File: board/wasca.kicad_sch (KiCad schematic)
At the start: 145 parts, among them CN1 UC09-0B16F00P11, CN2 CARTRIDGE_EDGE_CONNECTOR, CN3 TFP09-2-12B, CN4 SD-CARD 11P, CN5 2.54-1*8P母环保, SW1 TS-1101-C-W, SW2 TS-1101-C-W, U1 SN74LVC1T45DBVR, U10 74ALVC164245DGG:11-JSM, U11 W9825G6KH-6, U12 W9825G6KH-6, U13 SY8008CAAC, U14 SY8008CAAC, U15 XC6206P252MR, U16 LFE5U-25F-6BG256I, U17 P25Q16SH-SSH-IR, U2 SN74LVC1T45DBVR, U3 P25Q16SH-SSH-IR, U4 SN74LVC1T45DBVR, U5 SN74LVC1T45DBVR, U6 SN74LVC1T45DBVR, U7 74ALVC164245DGG:11-JSM, U8 74ALVC164245DGG:11-JSM, U9 RP2040, Y1 X322512MSB4SI, Y2 SX2M25.000M20F30TNN

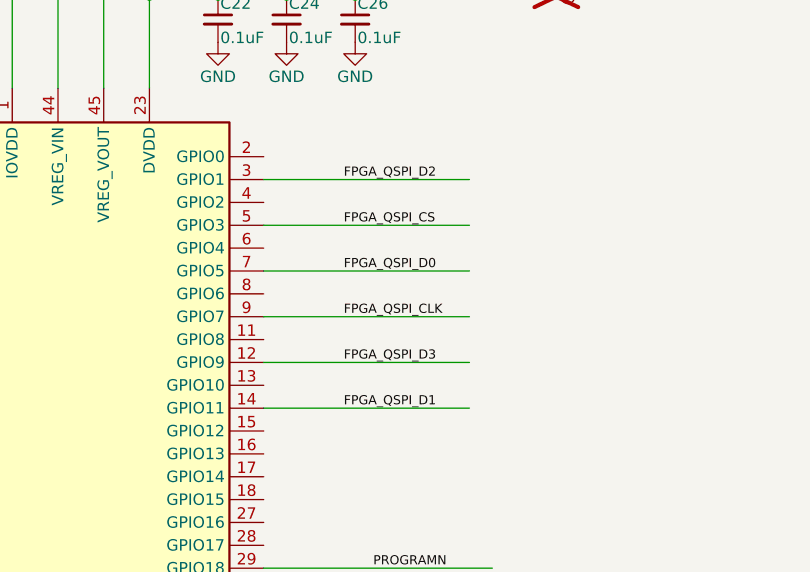
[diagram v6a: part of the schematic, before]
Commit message: Moving RP2040 to front to simplify 2-stage assembly (front at fab, back manually).
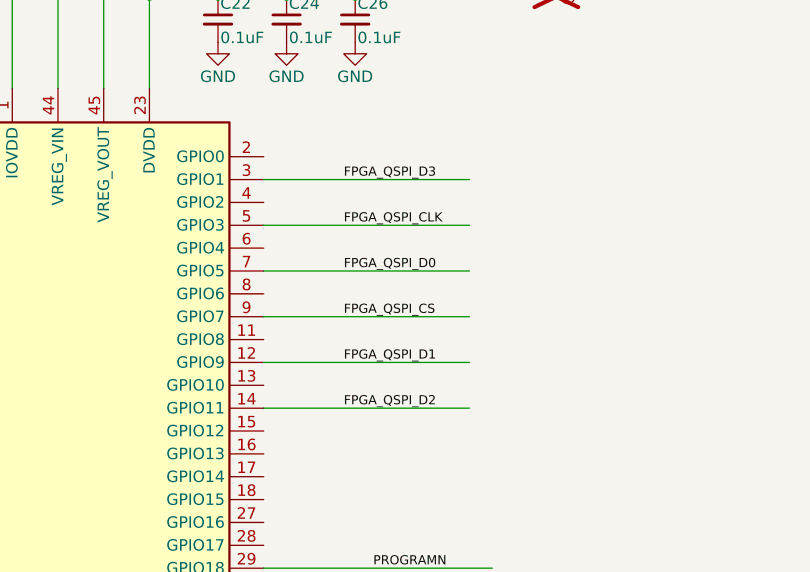
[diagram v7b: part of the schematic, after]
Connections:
- net FPGA_QSPI_CLK: now also U9.5 (GPIO3); no longer U9.9 (GPIO7)
- net FPGA_QSPI_CS: now also U9.9 (GPIO7); no longer U9.5 (GPIO3)
- net FPGA_QSPI_D1: now also U9.12 (GPIO9); no longer U9.14 (GPIO11)
- net FPGA_QSPI_D2: now also U9.14 (GPIO11); no longer U9.3 (GPIO1)
- net FPGA_QSPI_D3: now also U9.3 (GPIO1); no longer U9.12 (GPIO9)
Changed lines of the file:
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@@
 	(wire
 		(pts
+			(xy 250.19 575.31) (xy 273.05 575.31)
+		)
+		(stroke
+			(width 0)
+			(type default)
+		)
+	)
+	(wire
+		(pts
 			(xy 1078.23 104.14) (xy 1056.64 104.14)
 		)
@@
 	(wire
 		(pts
+			(xy 250.19 580.39) (xy 273.05 580.39)
+		)
+		(stroke
+			(width 0)
+			(type default)
+		)
+	)
+	(wire
+		(pts
 			(xy 190.5 445.77) (xy 190.5 439.42)
 		)
@@
 	(wire
 		(pts
+			(xy 250.19 554.99) (xy 273.05 554.99)
+		)
+		(stroke
+			(width 0)
+			(type default)
+		)
+	)
+	(wire
+		(pts
 			(xy 509.27 85.09) (xy 509.27 91.44)
 		)
@@
 	(wire
 		(pts
-			(xy 250.19 575.31) (xy 273.05 575.31)
-		)
-		(stroke
-			(width 0)
-			(type default)
-		)
-	)
-	(wire
-		(pts
 			(xy 938.53 283.21) (xy 960.12 283.21)
 		)
@@
 	(wire
 		(pts
-			(xy 250.19 580.39) (xy 273.05 580.39)
-		)
-		(stroke
-			(width 0)
-			(type default)
-		)
-	)
-	(wire
-		(pts
 			(xy 612.14 85.09) (xy 621.03 85.09)
 		)
@@
 	(wire
 		(pts
-			(xy 250.19 560.07) (xy 273.05 560.07)
-		)
-		(stroke
-			(width 0)
-			(type default)
-		)
-	)
-	(wire
-		(pts
 			(xy 233.68 153.67) (xy 252.73 153.67)
 		)
@@
 	(wire
 		(pts
-			(xy 250.19 554.99) (xy 273.05 554.99)
-		)
-		(stroke
-			(width 0)
-			(type default)
-		)
-	)
-	(wire
-		(pts
 			(xy 1055.37 405.13) (xy 1055.37 407.67)
 		)
@@
 	(wire
 		(pts
-			(xy 250.19 570.23) (xy 273.05 570.23)
-		)
-		(stroke
-			(width 0)
-			(type default)
-		)
-	)
-	(wire
-		(pts
 			(xy 621.03 74.93) (xy 621.03 76.2)
 		)
@@
 		)
 	)
+	(wire
+		(pts
+			(xy 250.19 570.23) (xy 273.05 570.23)
+		)
+		(stroke
+			(width 0)
+			(type default)
+		)
+	)
 	(bus
 		(pts
@@
 	(wire
 		(pts
+			(xy 250.19 560.07) (xy 273.05 560.07)
+		)
+		(stroke
+			(width 0)
+			(type default)
+		)
+	)
+	(wire
+		(pts
 			(xy 542.29 74.93) (xy 542.29 80.01)
 		)
@@
 		)
 	)
-	(label "FPGA_QSPI_D1"
-		(at 259.08 580.39 0)
-		(effects
-			(font
-				(size 1.016 1.016)
-			)
-			(justify left bottom)
-		)
-	)
-	(label "FPGA_QSPI_D3"
-		(at 259.08 575.31 0)
-		(effects
-			(font
-				(size 1.016 1.016)
-			)
-			(justify left bottom)
-		)
-	)
 	(label "ABUS_3V_A22"
 		(at 238.76 158.75 0)
@@
 		)
 	)
-	(label "FPGA_QSPI_D2"
-		(at 259.08 554.99 0)
-		(effects
-			(font
-				(size 1.016 1.016)
-			)
-			(justify left bottom)
-		)
-	)
 	(label "+5V_SATURN"
 		(at 72.39 363.22 180)
@@
 		)
 	)
+	(label "FPGA_QSPI_D1"
+		(at 259.08 575.31 0)
+		(effects
+			(font
+				(size 1.016 1.016)
+			)
+			(justify left bottom)
+		)
+	)
 	(label "SDRAM2_A2"
 		(at 750.57 133.35 180)
@@
 		)
 	)
+	(label "FPGA_QSPI_D2"
+		(at 259.08 580.39 0)
+		(effects
+			(font
+				(size 1.016 1.016)
+			)
+			(justify left bottom)
+		)
+	)
 	(label "FPGA_QSPI_CS"
 		(at 741.68 74.93 0)
@@
 		)
 	)
+	(label "FPGA_QSPI_CS"
+		(at 259.08 570.23 0)
+		(effects
+			(font
+				(size 1.016 1.016)
+			)
+			(justify left bottom)
+		)
+	)
 	(label "ABUS_3V_D12"
 		(at 255.27 325.12 0)
@@
 		)
 	)
+	(label "FPGA_QSPI_CLK"
+		(at 259.08 560.07 0)
+		(effects
+			(font
+				(size 1.016 1.016)
+			)
+			(justify left bottom)
+		)
+	)
 	(label "SDRAM1_A5"
 		(at 410.21 300.99 180)
@@
 		)
 	)
+	(label "FPGA_QSPI_D3"
+		(at 259.08 554.99 0)
+		(effects
+			(font
+				(size 1.016 1.016)
+			)
+			(justify left bottom)
+		)
+	)
 	(label "SDRAM2_DQ5"
 		(at 750.57 87.63 180)
@@
 		)
 	)
-	(label "FPGA_QSPI_CLK"
-		(at 259.08 570.23 0)
-		(effects
-			(font
-				(size 1.016 1.016)
-			)
-			(justify left bottom)
-		)
-	)
 	(label "ABUS_A5"
 		(at 142.24 170.18 0)
@@
 		)
 	)
-	(label "FPGA_QSPI_CS"
-		(at 259.08 560.07 0)
-		(effects
-			(font
-				(size 1.016 1.016)
-			)
-			(justify left bottom)
-		)
-	)

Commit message: Small board updates
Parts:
- D4: footprint LED_SMD:LED_0603_1608Metric -> wasca:LED_0805
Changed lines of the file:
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@@
 			)
 		)
-		(property "Footprint" "LED_SMD:LED_0603_1608Metric"
+		(property "Footprint" "wasca:LED_0805"
 			(at 621.03 100.33 0)
 			(hide yes)
